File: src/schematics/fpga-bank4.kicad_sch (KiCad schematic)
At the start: 1 part

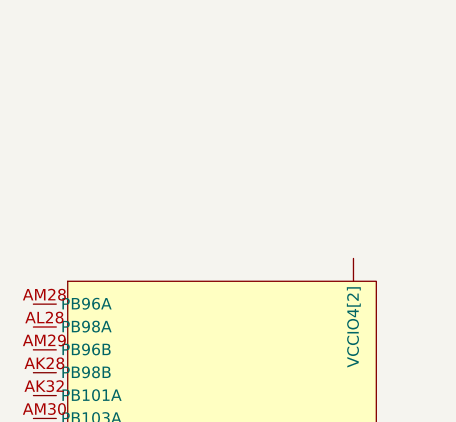
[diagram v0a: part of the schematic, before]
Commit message: Draft connections between the FPGA and the memories
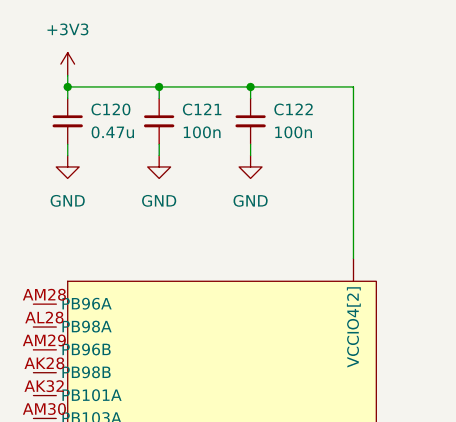
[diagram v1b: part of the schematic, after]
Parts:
- added C120: 0.47u, symbol Device:C_Small
- added C121, C122: 100n, symbol Device:C_Small
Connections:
- net VCCIO4 renamed +3V3
- net +3V3: now also C120.1, C121.1, C122.1
- new net GND: C120.2, C121.2, C122.2

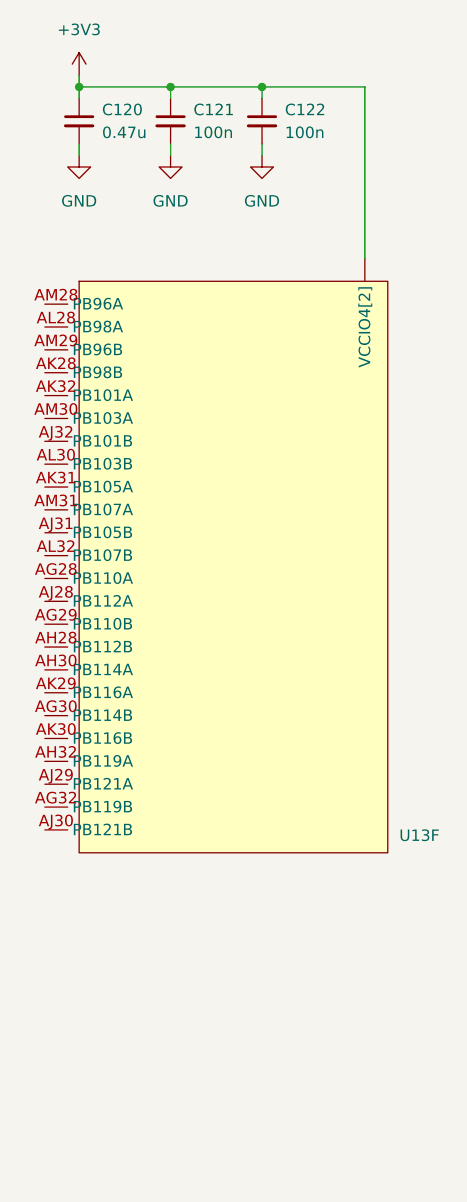
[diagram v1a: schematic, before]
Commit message: Adds draft of IO connector schematic connections to FPGA
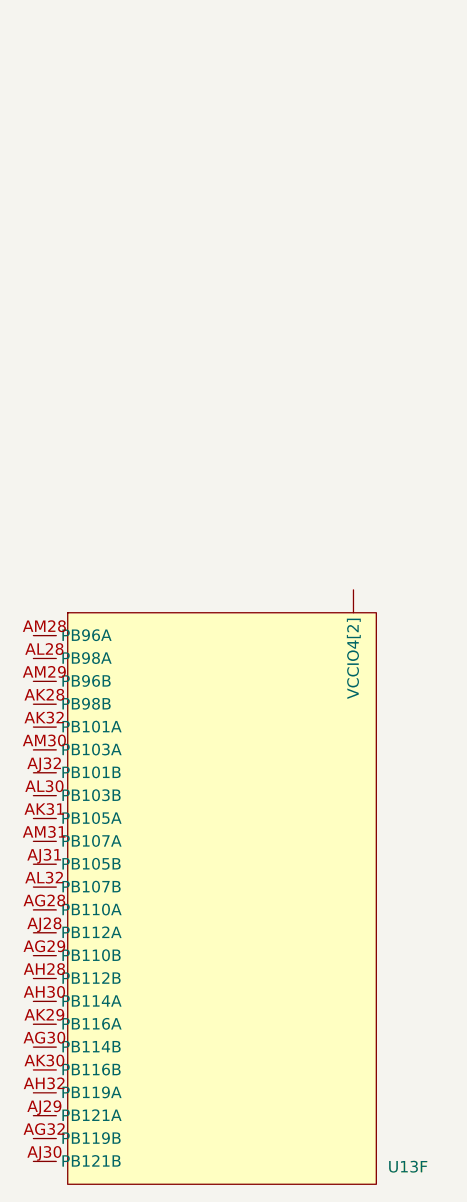
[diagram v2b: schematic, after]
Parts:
- removed C120: 0.47u, symbol Device:C_Small
- removed C121, C122: 100n, symbol Device:C_Small
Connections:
- net +3V3 renamed VCCIO4
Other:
- moved on the sheet: U13F

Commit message: Adds the clock oscillator
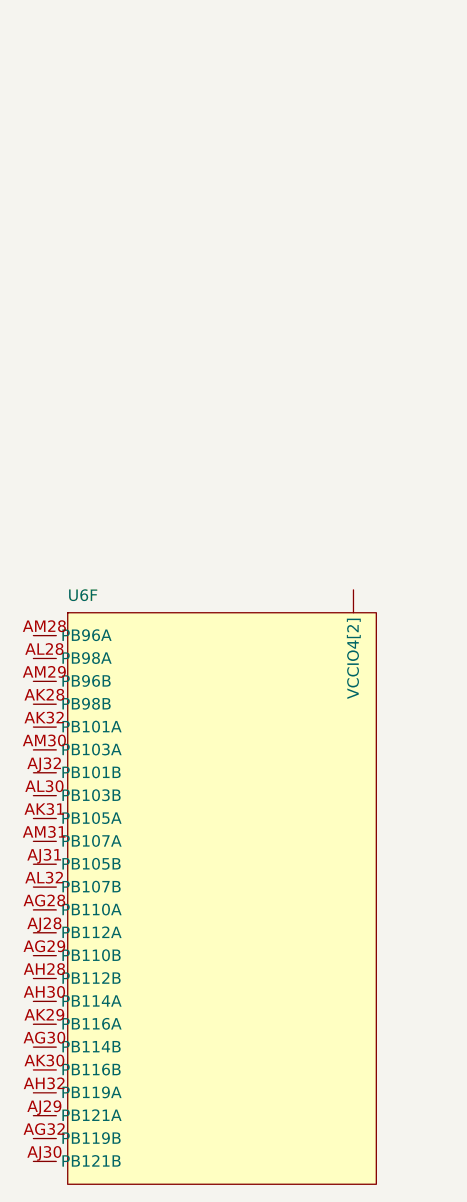
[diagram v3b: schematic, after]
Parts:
- removed U13: ~, symbol ECAP5-BSOM:LFE5U-85F-*BG756*
- added U6: ~, symbol ECAP5-BSOM:LFE5U-85F-*BG756*
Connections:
- net VCCIO4: now also U6. (VCCIO4[2]), U6.AB23 (VCCIO4), U6.AC23 (VCCIO4)
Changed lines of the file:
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@@
 		(on_board yes)
 		(dnp no)
-		(fields_autoplaced yes)
-		(property "Reference" "U13"
-			(at 171.45 130.1749 0)
+		(property "Reference" "U6"
+			(at 135.89 66.6749 0)
 			(effects
 				(font
@@
 			(project "ecap5-bsom"
 				(path "/c5fd18a3-9aa0-4151-b6e0-94da3d606686/9ec64d27-698a-408d-bb9c-7e381193a80d/ce582390-3a89-4130-936e-5664e8586325"
-					(reference "U13")
+					(reference "U6")
 					(unit 6)
 				)

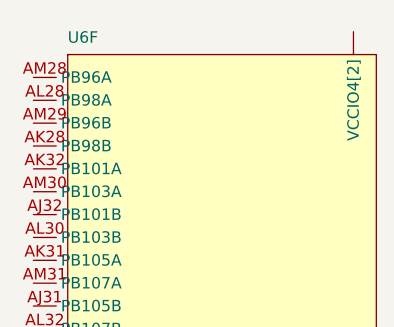
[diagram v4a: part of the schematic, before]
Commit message: Fix some ERC issues
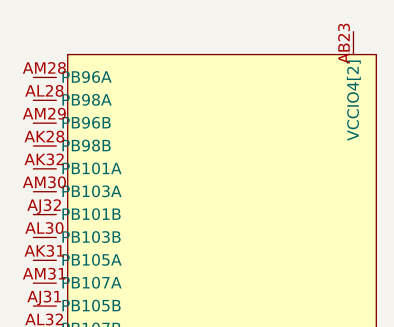
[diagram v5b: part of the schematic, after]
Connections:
- net VCCIO4: no longer names the net of U6.AB23 (VCCIO4[2]), U6.AC23 (VCCIO4)
- net VCCIO4: no longer U6. (VCCIO4[2])
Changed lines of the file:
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@@
 				)
 				(justify left)
+				(hide yes)
 			)
 		)
@@
 		(pin "Y31"
 		)
-		(pin ""
-		)
 		(pin "A10"
 		)
@@
 		(pin "Y32"
 		)
-		(pin ""
-		)
 		(pin "AB23"
 		)
@@
 		(pin "K16"
 		)
-		(pin ""
-		)
 		(pin "A18"
 		)
@@
 		(pin "K21"
 		)
-		(pin ""
-		)
 		(pin "B32"
 		)
@@
 		(pin "T23"
 		)
-		(pin ""
-		)
 		(pin "AA23"
 		)
@@
 		(pin "AM31"
 		)
-		(pin ""
-		)
 		(pin "AA10"
 		)
@@
 		(pin "Y7"
 		)
-		(pin ""
-		)
 		(pin "B1"
 		)
@@
 		(pin "T10"
 		)
-		(pin ""
-		)
 		(pin "AB10"
 		)
@@
 		(pin "M14"
 		)
-		(pin ""
-		)
 		(pin "AH12"
 		)
@@
 		(pin "V19"
 		)
-		(pin ""
-		)
 		(pin "AC11"
 		)
@@
 		(pin "AA11"
 		)
-		(pin ""
-		)
 		(instances

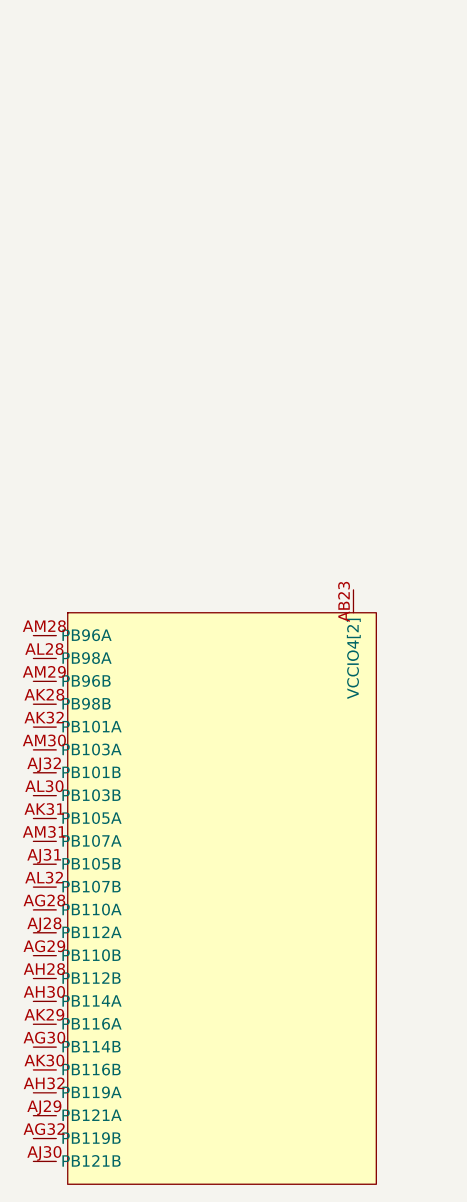
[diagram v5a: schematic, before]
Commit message: Fixes bus aliases
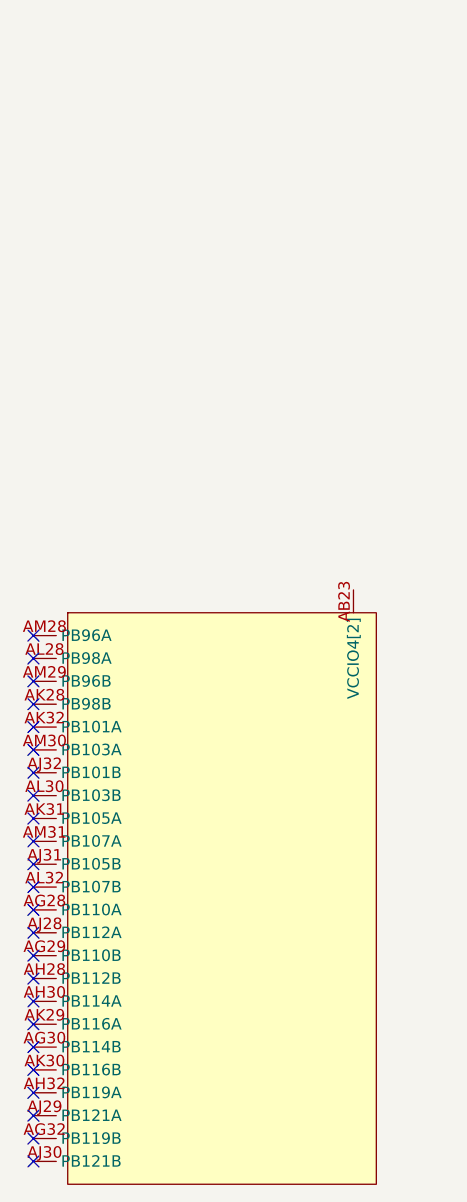
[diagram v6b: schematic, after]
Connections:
- no-connect marks 0 -> 24
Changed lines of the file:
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@@
 		(comment 3 "${Part Number}")
+	)
+	(no_connect
+		(at 132.08 124.46)
+	)
+	(no_connect
+		(at 132.08 129.54)
+	)
+	(no_connect
+		(at 132.08 101.6)
+	)
+	(no_connect
+		(at 132.08 76.2)
+	)
+	(no_connect
+		(at 132.08 121.92)
+	)
+	(no_connect
+		(at 132.08 99.06)
+	)
+	(no_connect
+		(at 132.08 106.68)
+	)
+	(no_connect
+		(at 132.08 109.22)
+	)
+	(no_connect
+		(at 132.08 114.3)
+	)
+	(no_connect
+		(at 132.08 93.98)
+	)
+	(no_connect
+		(at 132.08 116.84)
+	)
+	(no_connect
+		(at 132.08 96.52)
+	)
+	(no_connect
+		(at 132.08 73.66)
+	)
+	(no_connect
+		(at 132.08 91.44)
+	)
+	(no_connect
+		(at 132.08 86.36)
+	)
+	(no_connect
+		(at 132.08 119.38)
+	)
+	(no_connect
+		(at 132.08 71.12)
+	)
+	(no_connect
+		(at 132.08 111.76)
+	)
+	(no_connect
+		(at 132.08 78.74)
+	)
+	(no_connect
+		(at 132.08 104.14)
+	)
+	(no_connect
+		(at 132.08 83.82)
+	)
+	(no_connect
+		(at 132.08 88.9)
+	)
+	(no_connect
+		(at 132.08 127)
+	)
+	(no_connect
+		(at 132.08 81.28)
 	)
 	(symbol
@@
 		(pin "AB32"
 		)
-		(pin "AB32"
+		(pin "AB31"
 		)
 		(pin "AC26"
